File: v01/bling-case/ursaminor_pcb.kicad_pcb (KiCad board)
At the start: 2 copper layers, 298.6 x 118.1 mm, 210 parts, among them J1 USB_C_Receptacle_USB2.0, J2 I2C-L, J3 I2C-R, J4 AVR-ISP-6, SW1 Reset, U1 ATmega32U4-AU, U2 MCP23017_SO, U3 IS31FL3733-TQ, U4 IS31FL3733-TQ, U5 PRTR5V0U2X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

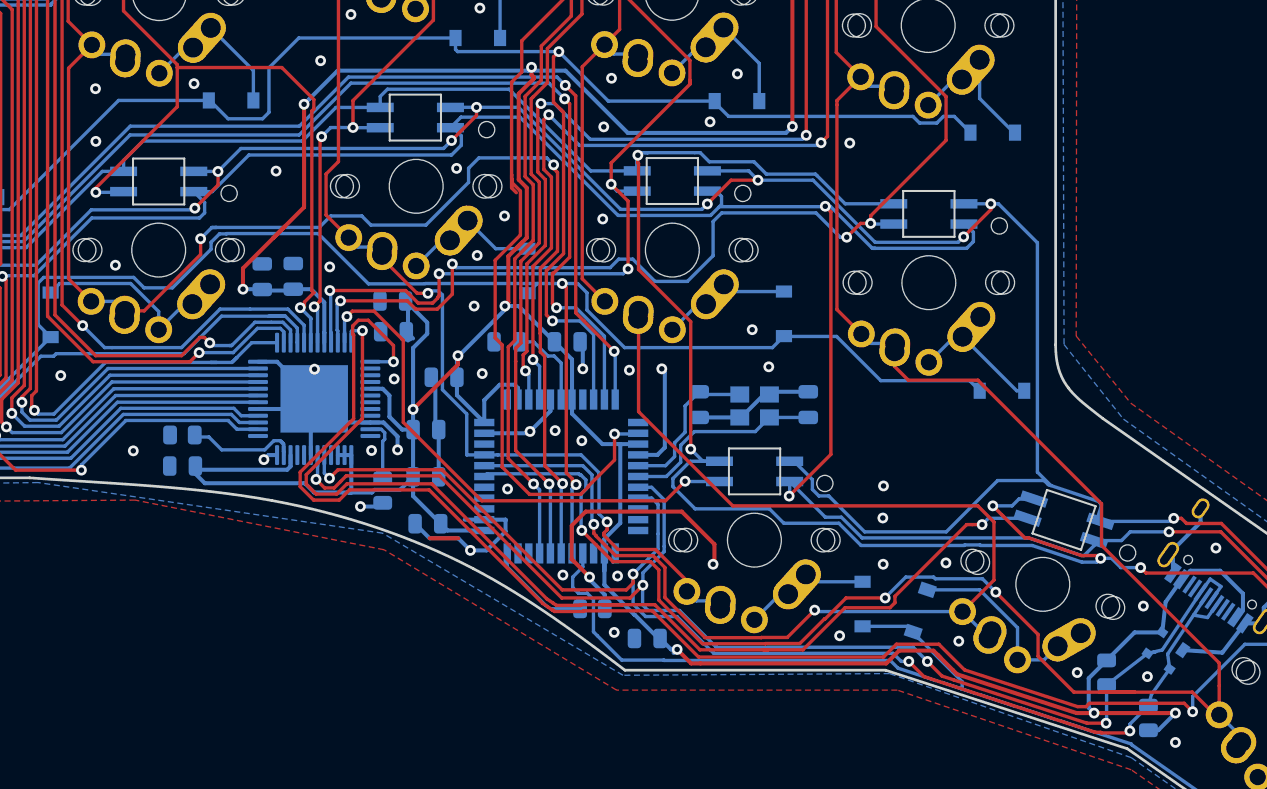
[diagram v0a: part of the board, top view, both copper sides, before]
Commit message: Get left side routed.
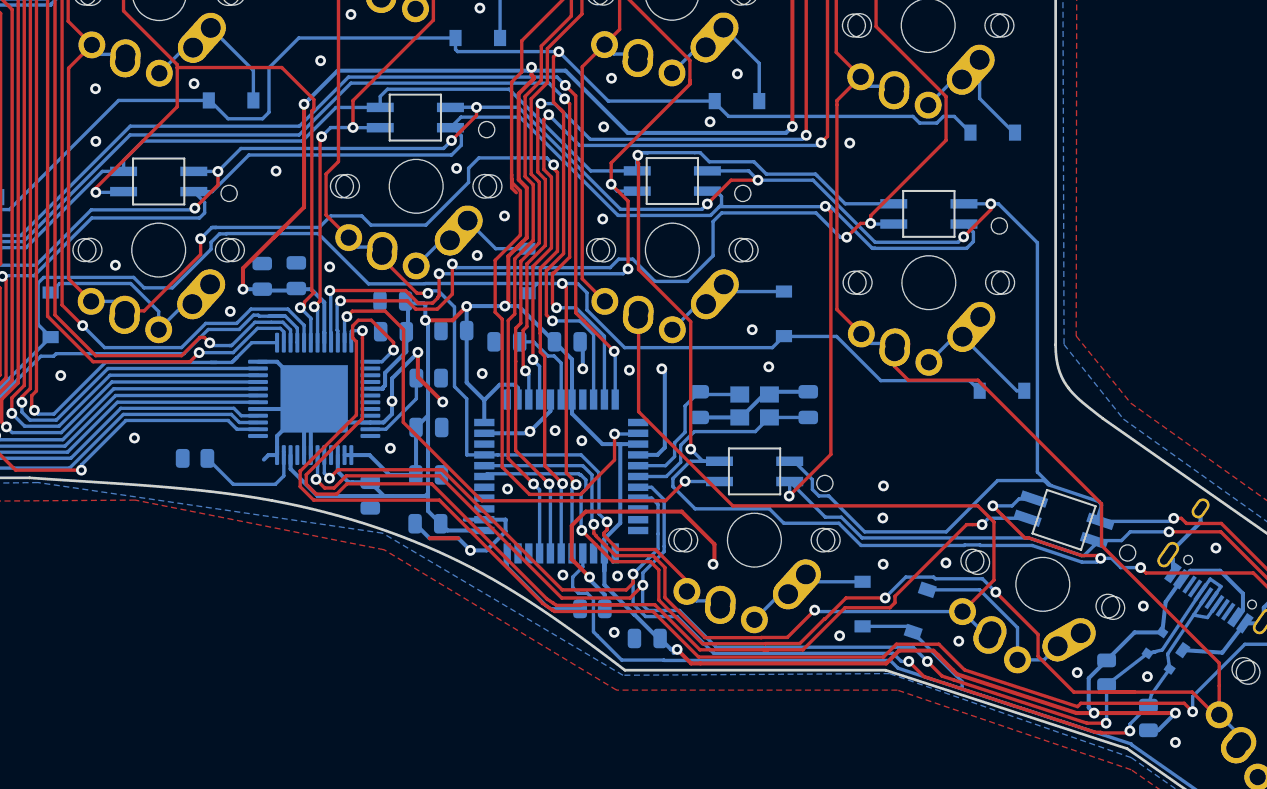
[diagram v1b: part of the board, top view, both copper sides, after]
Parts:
- moved C11 18.5 mm to (81.5, 100.2), turned to 180 degrees
- moved C21 18.1 mm to (77.1, 105.2), turned to 90 degrees
- moved C17 17.8 mm to (81.5, 103.7), turned to 0 degrees
- moved C18 17.7 mm to (71.7, 88.9), turned to 270 degrees
- moved C12 16.6 mm to (69.1, 89.0), turned to 270 degrees
- moved R14 9.00 mm to (81.5, 96.5), turned to 0 degrees
- moved C6 3.53 mm to (83.3, 93.0)
- moved R12 1.97 mm to (64.1, 102.5)
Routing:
- net GND: track 138.4 -> 145.9 mm, vias 99 -> 97
- net +5V: track 411.3 -> 407.0 mm
- net Net-(R14-Pad1): track 4.60 -> 5.87 mm
- net Left-CS9: track 105.7 -> 104.9 mm

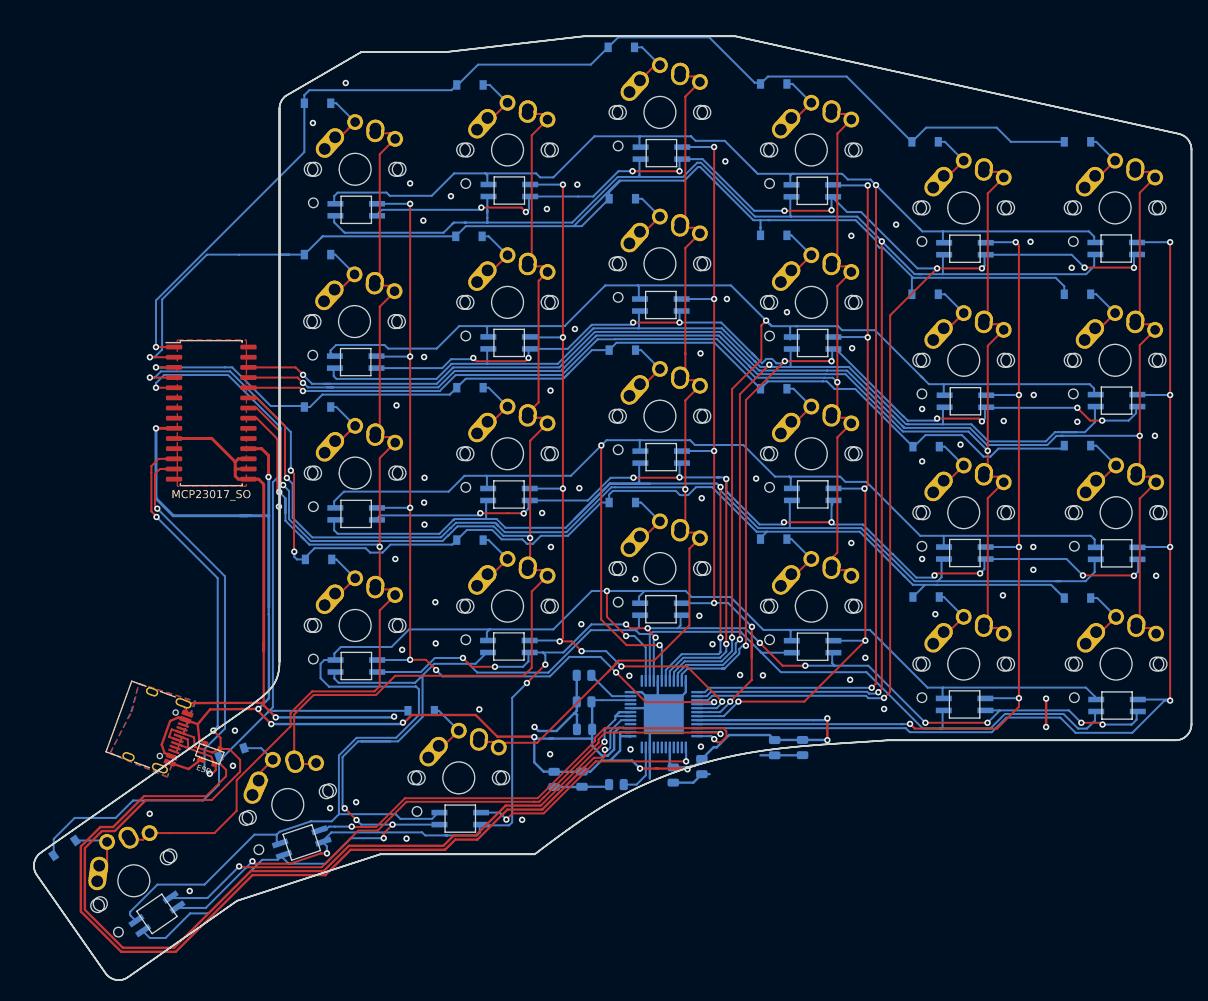
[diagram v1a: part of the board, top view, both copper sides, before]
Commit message: Clean up right side and roughly place components.
Still need to figure out the right side LED driver.
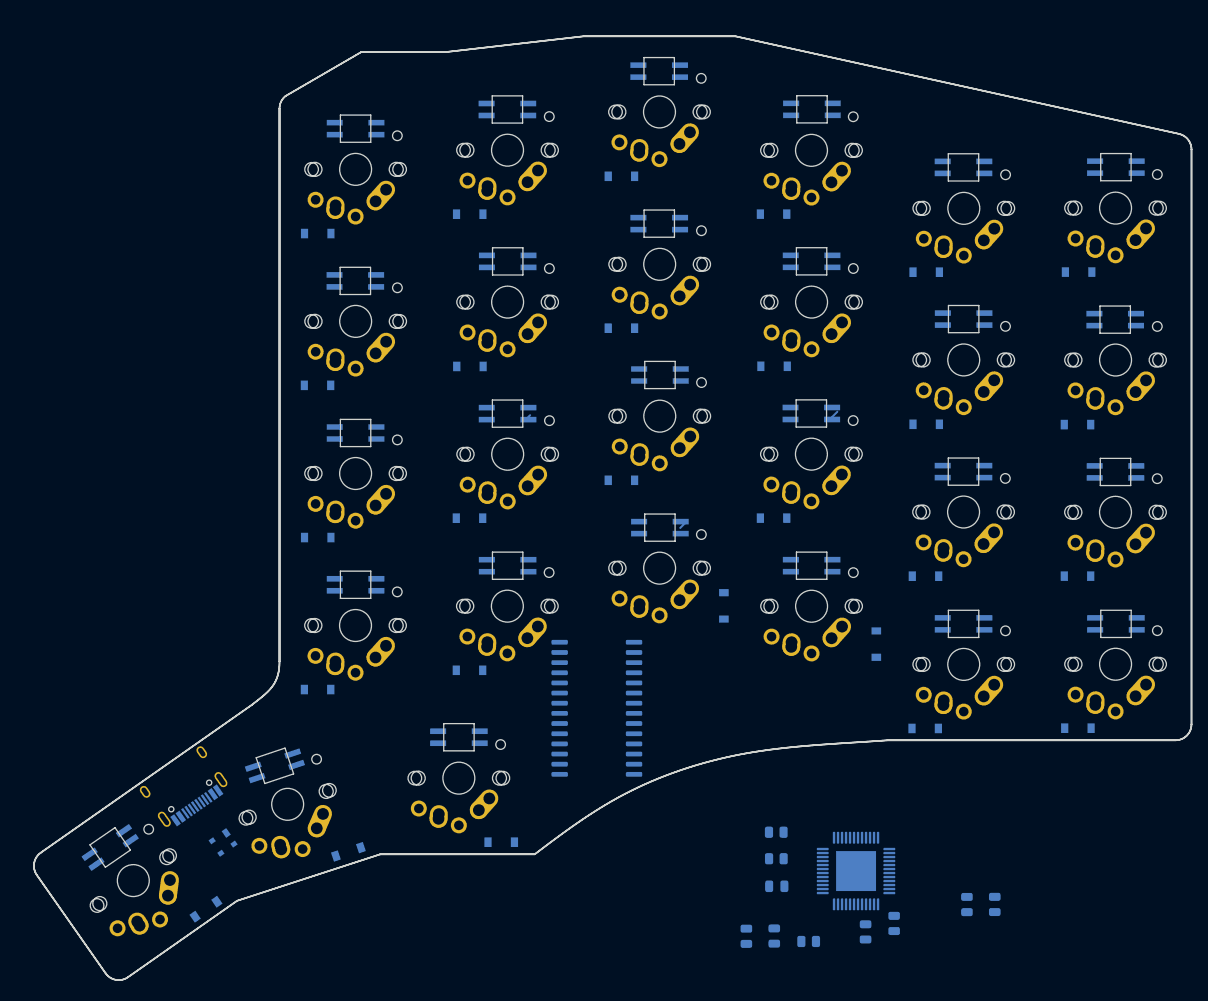
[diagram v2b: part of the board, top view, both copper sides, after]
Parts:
- J3, U2, U7: moved to B.Cu
- moved U2 60.7 mm to (238.2, 99.8), turned to 180 degrees
- moved C14 31.0 mm to (260.4, 128.2)
- moved C9 31.0 mm to (284.5, 124.3)
- moved R13 31.0 mm to (264.7, 128.9)
- moved R9 31.0 mm to (260.6, 118.6)
- moved C20 31.0 mm to (260.7, 122.0)
- moved R10 31.0 mm to (260.6, 115.3)
- moved C8 31.0 mm to (256.9, 128.3)
- moved C10 31.0 mm to (275.4, 126.7)
- moved C15 31.0 mm to (287.9, 124.3)
- moved C16 31.0 mm to (271.8, 127.7)
- moved U3 31.0 mm to (270.6, 120.1)
- moved D52 19.3 mm to (189.3, 124.9)
- moved D54 19.2 mm to (226.2, 116.5)
- moved D53 19.2 mm to (207.1, 117.7)
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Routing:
- net VBUS: track 220.7 -> 0.00 mm, vias 10 -> 0
- net Right-SW1: track 211.8 -> 0.22 mm, vias 2 -> 0
- net Right-SW2: track 204.6 -> 0.90 mm, vias 4 -> 0
- net Right-SW11: track 198.9 -> 0.00 mm, vias 2 -> 0
- net Right-SW10: track 197.5 -> 0.00 mm, vias 2 -> 0
- net Right-SW12: track 192.2 -> 0.00 mm, vias 11 -> 0
- net Right-SW3: track 191.7 -> 0.00 mm, vias 15 -> 0
- net Col11: track 190.9 -> 0.07 mm, vias 2 -> 0
- net Col8: track 187.1 -> 0.40 mm, vias 2 -> 0
- net SCL-R: track 174.4 -> 0.00 mm, vias 3 -> 0
- net SDA-R: track 174.2 -> 0.00 mm, vias 3 -> 0
- net Col10: track 171.2 -> 0.22 mm, vias 2 -> 0
- net Col7: track 171.5 -> 0.68 mm, vias 2 -> 0
- net Right-SW8: track 165.9 -> 0.00 mm, vias 2 -> 0
- net Right-SW7: track 165.8 -> 0.00 mm, vias 2 -> 0
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- removed copper zone on B.Cu, net VSS
- removed copper zone on F.Cu, net VSS

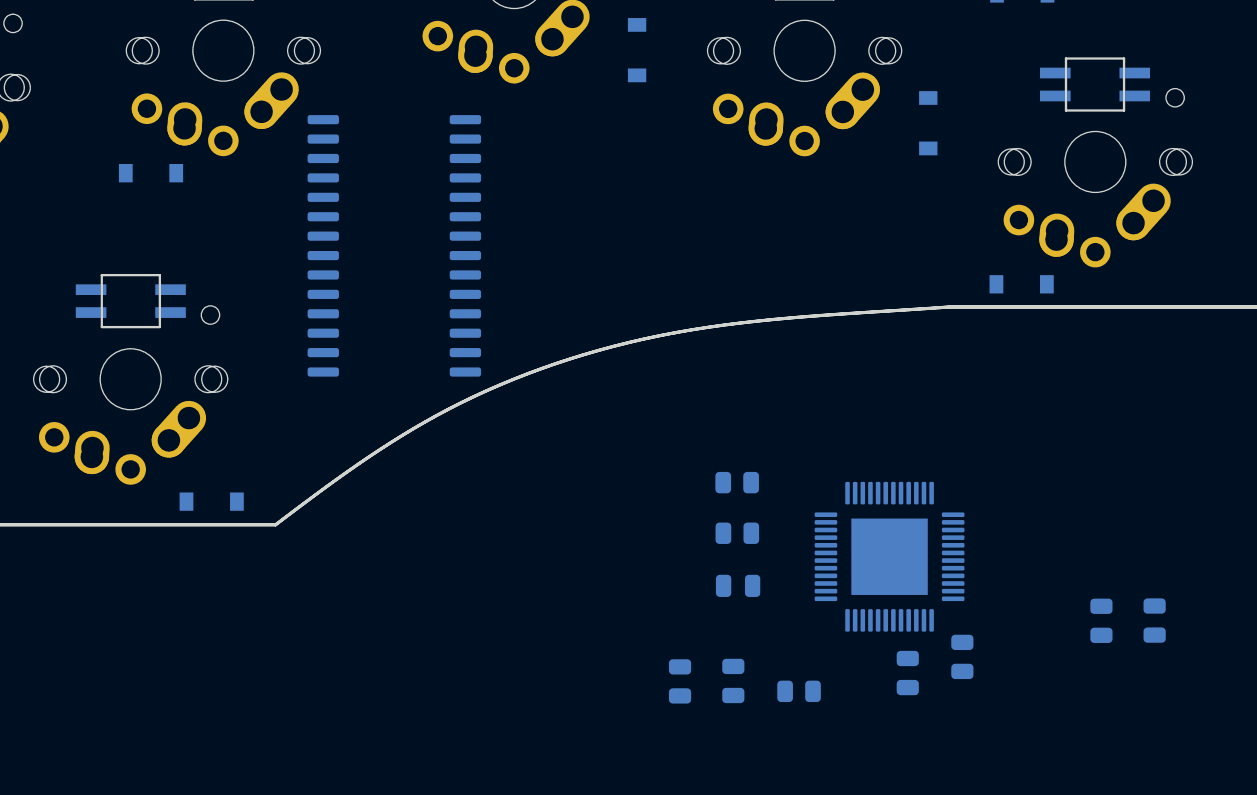
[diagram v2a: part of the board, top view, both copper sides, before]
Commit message: First draft of complete right side placements
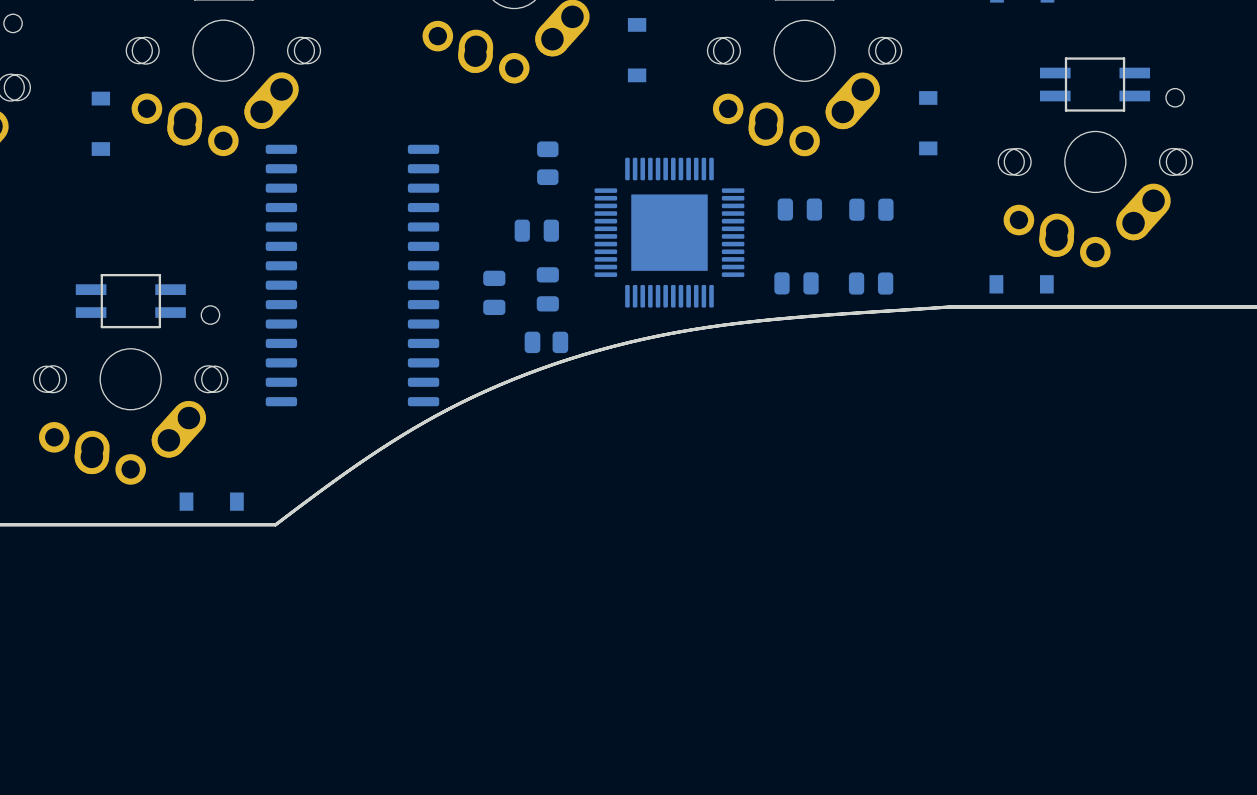
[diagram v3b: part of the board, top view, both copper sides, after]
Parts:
- removed R9: 100K, Resistor_SMD:R_0805_2012Metric
- moved C15 35.5 mm to (264.7, 97.4), turned to 180 degrees
- moved C9 30.8 mm to (269.4, 97.4), turned to 180 degrees
- moved C14 28.3 mm to (248.2, 102.6)
- moved R13 28.2 mm to (248.1, 106.1)
- moved C8 28.2 mm to (244.7, 102.8)
- moved C20 26.7 mm to (247.5, 98.8)
- moved C16 26.5 mm to (264.5, 102.2), turned to 180 degrees
- moved U3 25.6 mm to (256.2, 98.9)
- moved C10 25.1 mm to (269.4, 102.2), turned to 0 degrees
- moved R10 24.3 mm to (248.2, 94.4), turned to 90 degrees
- moved D47 4.60 mm to (219.0, 91.8), turned to 90 degrees
- moved U2 3.36 mm to (235.4, 101.7), turned to 0 degrees

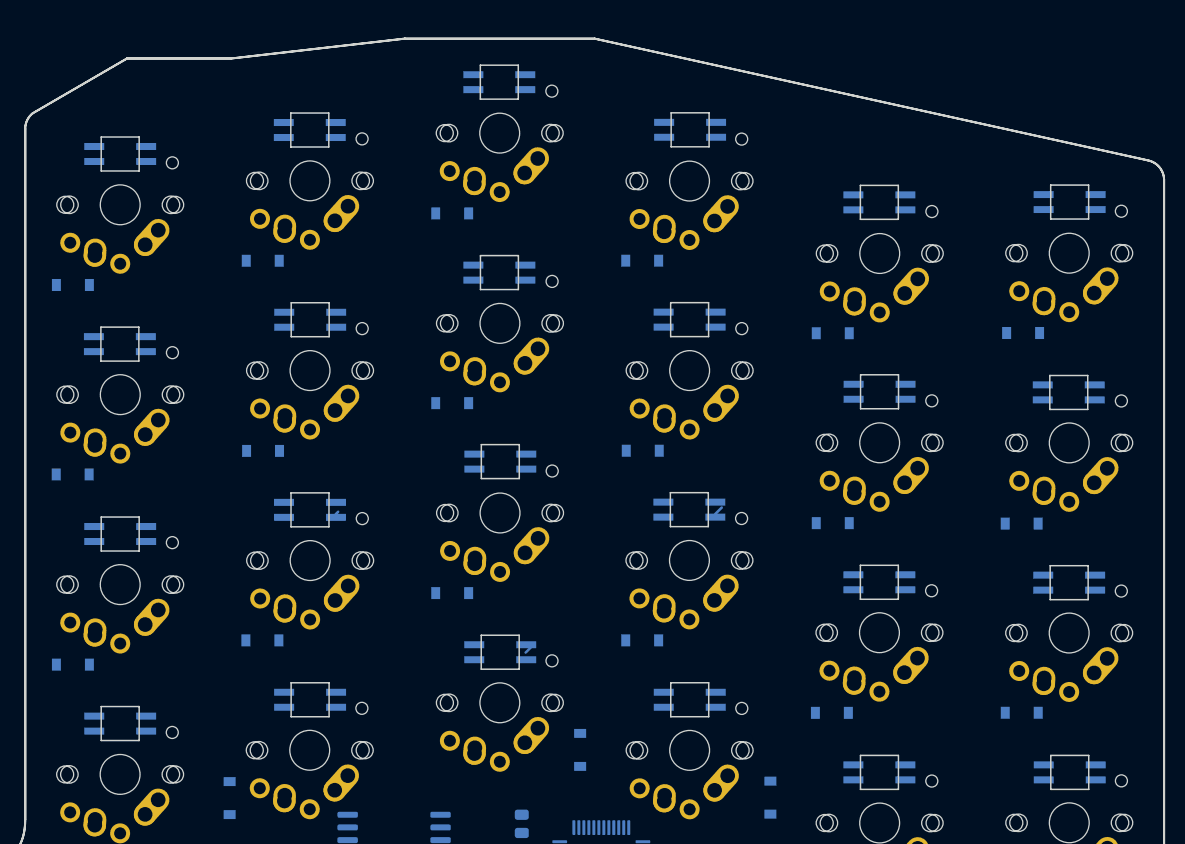
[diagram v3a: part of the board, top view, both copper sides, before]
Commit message: Top row of right LEDs and LED columns are done.
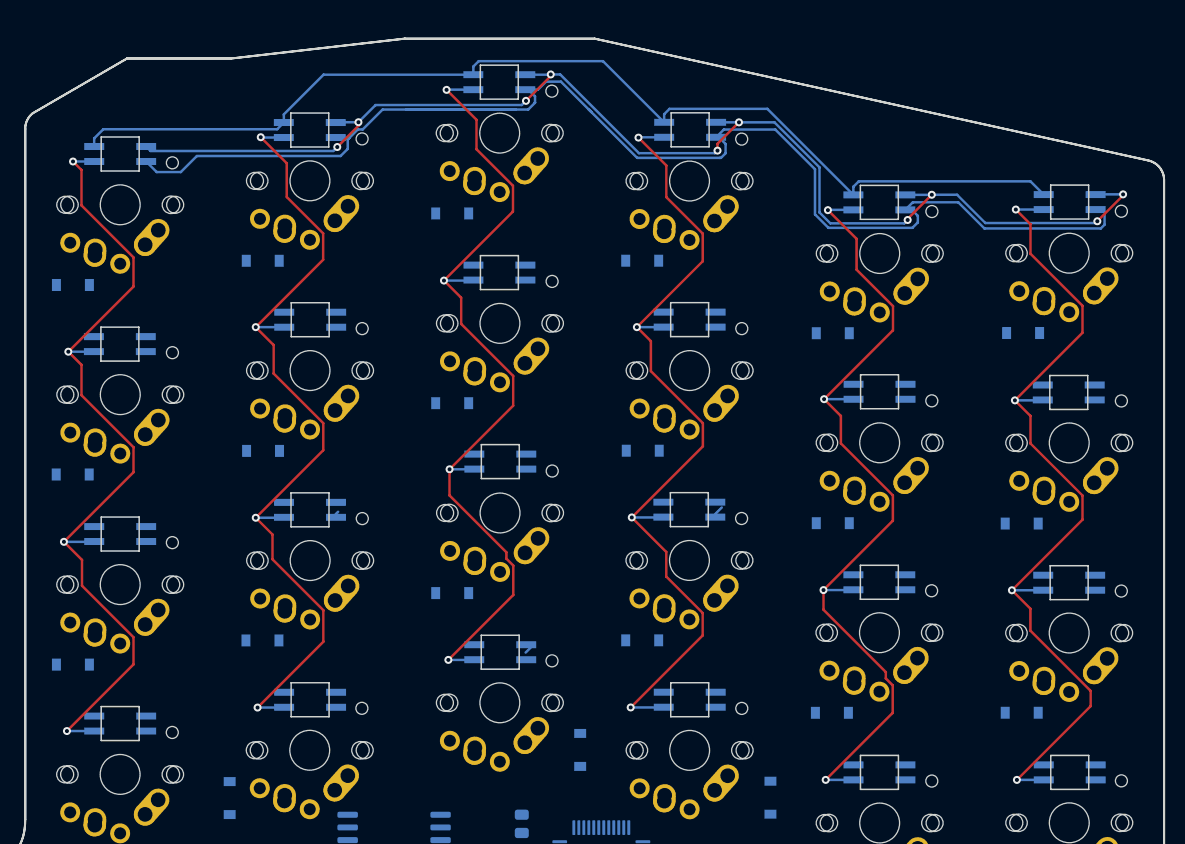
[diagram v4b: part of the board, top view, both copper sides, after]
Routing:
- net Right-SW10: track 0.00 -> 138.6 mm
- net Right-SW11: track 0.00 -> 129.5 mm, vias 0 -> 10
- net Right-SW12: track 0.00 -> 108.7 mm
- net Right-CS6: track 0.00 -> 86.1 mm, vias 0 -> 4
- net Right-CS4: track 0.00 -> 85.8 mm, vias 0 -> 4
- net Right-CS5: track 0.00 -> 85.3 mm, vias 0 -> 4
- net Right-CS2: track 0.00 -> 84.3 mm, vias 0 -> 4
- net Right-CS3: track 0.00 -> 84.3 mm, vias 0 -> 4
- net Right-CS1: track 0.00 -> 83.9 mm, vias 0 -> 4
